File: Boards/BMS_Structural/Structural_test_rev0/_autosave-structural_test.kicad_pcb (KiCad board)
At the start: 2 copper layers, 43.8 x 69.7 mm, 9 parts, among them J1 MM_F_VT_08, Q1 LMT85-Q1, Q2 LMT85-Q1

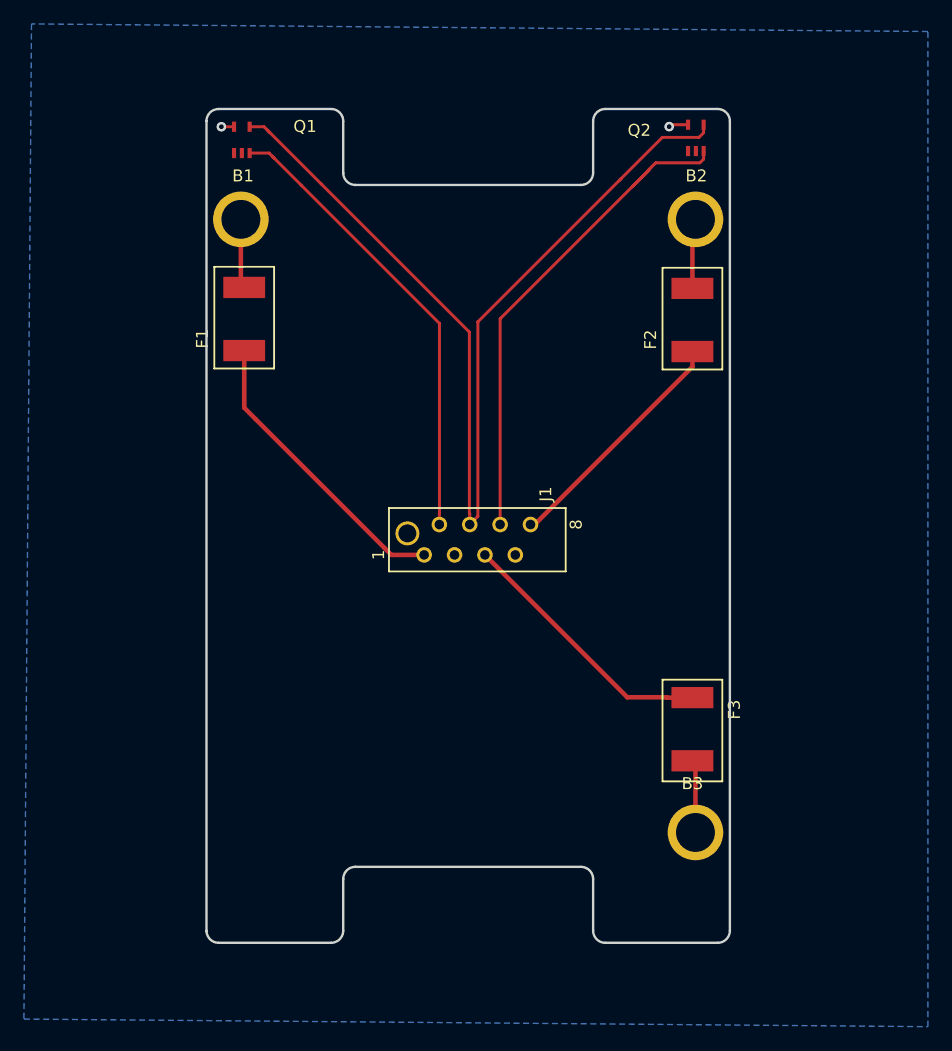
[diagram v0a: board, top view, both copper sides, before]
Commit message: Exported gerbers for structural test rev0; Updated BMS peripheral schematic for 2 temp sensors per module and added connectors
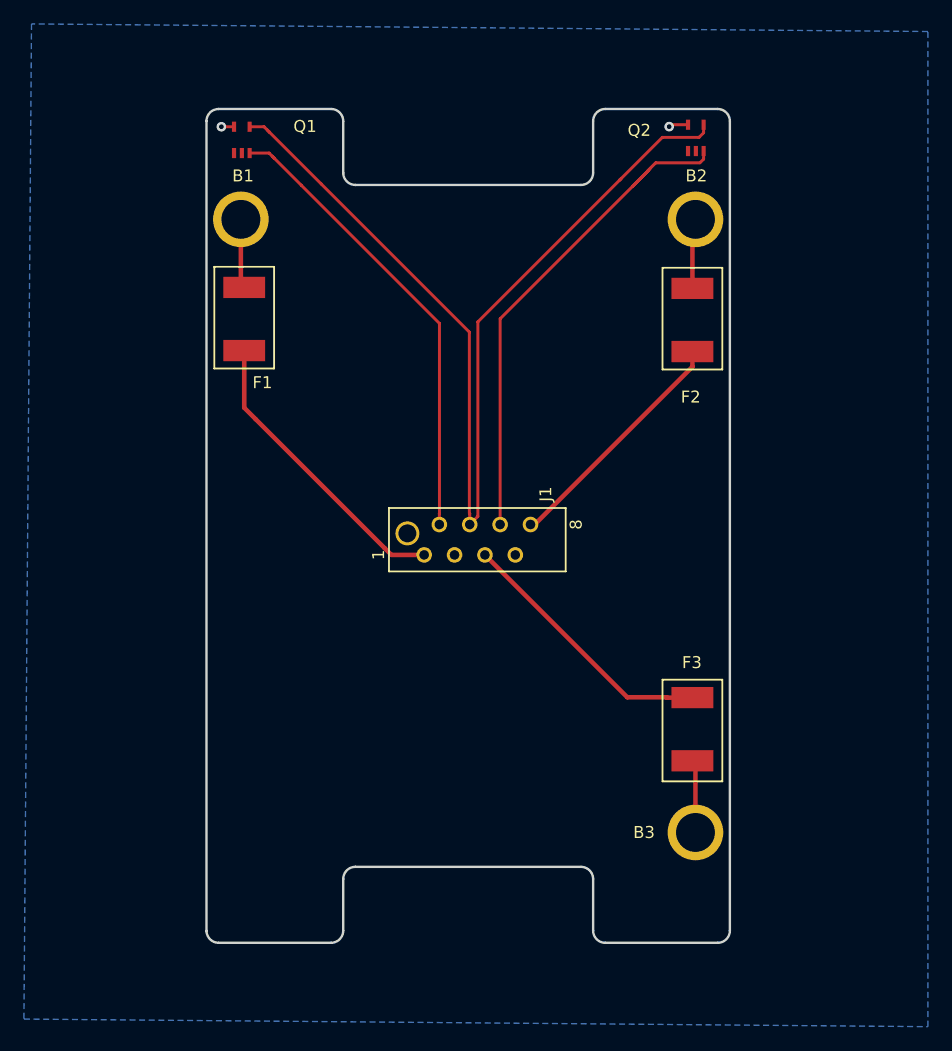
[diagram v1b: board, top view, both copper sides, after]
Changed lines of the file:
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@@
   )
   (setup
-    (last_trace_width 0.381)
+    (last_trace_width 0.25)
     (user_trace_width 0.381)
     (trace_clearance 0.2)
@@
     (visible_elements 7FFFFFFF)
     (pcbplotparams
-      (layerselection 0x010fc_ffffffff)
-      (usegerberextensions false)
+      (layerselection 0x010a8_ffffffff)
+      (usegerberextensions true)
       (usegerberattributes false)
       (usegerberadvancedattributes false)
@@
       (outputformat 1)
       (mirror false)
-      (drillshape 1)
+      (drillshape 0)
       (scaleselection 1)
-      (outputdirectory ""))
+      (outputdirectory "gerbers_v0/"))
   )
   (net 0 "")
@@
   (module footprints:Bolt_connect_4-40_round (layer F.Cu)
     (at 106.3 136.8)
-    (fp_text reference B3 (at -0.255 -4.085) (layer F.SilkS)
+    (fp_text reference B3 (at -4.3 0) (layer F.SilkS)
       (effects (font (size 1 1) (thickness 0.15)))
     )
@@
   (module footprints:Fuse_1812 (layer F.Cu)
     (at 68.58 96.52 90)
-    (fp_text reference F1 (at 1 -3.5 90) (layer F.SilkS)
+    (fp_text reference F1 (at -2.68 1.52 180) (layer F.SilkS)
       (effects (font (size 1 1) (thickness 0.15)))
     )
@@
   (module footprints:Fuse_1812 (layer F.Cu)
     (at 106.045 96.6 90)
-    (fp_text reference F2 (at 1 -3.5 90) (layer F.SilkS)
+    (fp_text reference F2 (at -3.8 -0.145 180) (layer F.SilkS)
       (effects (font (size 1 1) (thickness 0.15)))
     )
@@
   (module footprints:Fuse_1812 (layer F.Cu)
     (at 106.045 125.53 270)
-    (fp_text reference F3 (at 1 -3.5 270) (layer F.SilkS)
-      (effects (font (size 1 1) (thickness 0.15)))
-    )
+    (fp_text reference F3 (at -2.93 0.045) (layer F.SilkS)
+      (effects (font (size 1 1) (thickness 0.15)))
+    )
